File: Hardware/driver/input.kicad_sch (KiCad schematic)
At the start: 20 parts

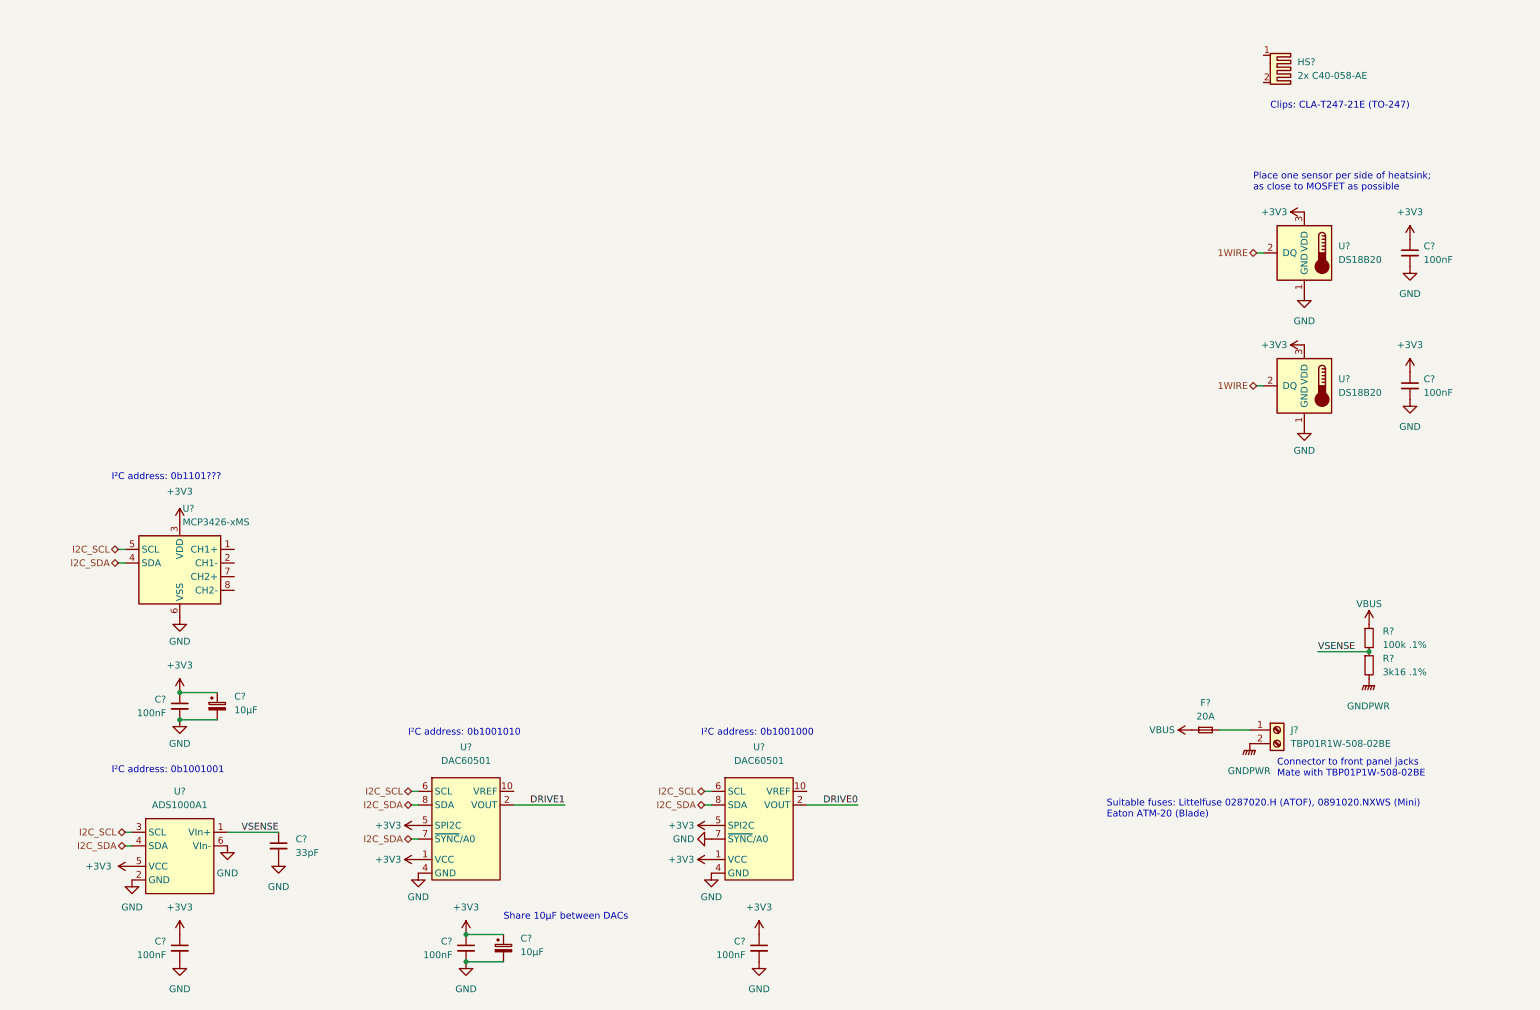
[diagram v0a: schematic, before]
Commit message: Basic board layout shape
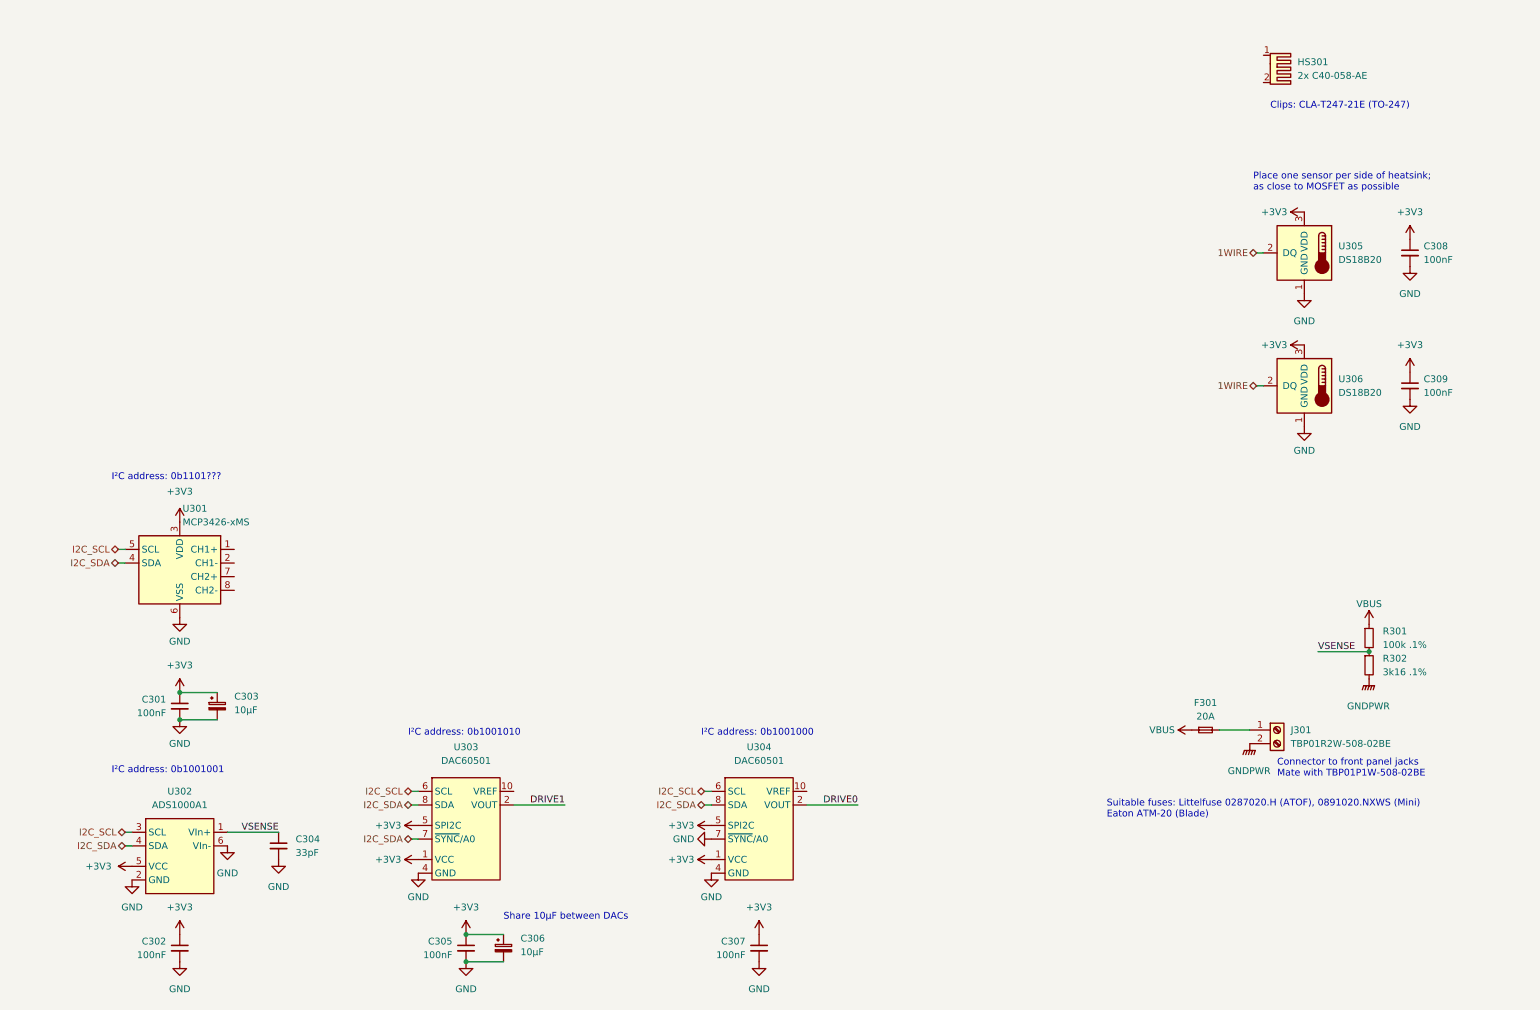
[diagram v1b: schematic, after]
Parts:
- J301: renamed from J?; value TBP01R1W-508-02BE -> TBP01R2W-508-02BE; footprint programmable-load:CUI_TBP01R1W-508-02BE -> programmable-load:CUI_TBP01R2W-508-02BE
- gave numbers to parts that had none: 19

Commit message: Added mains supply input
- The driver board contains a switching mains supply that will give us
  the 12V the system needs, as if by magic

- More work on layout, basically placed the output MOSFETs and stuff
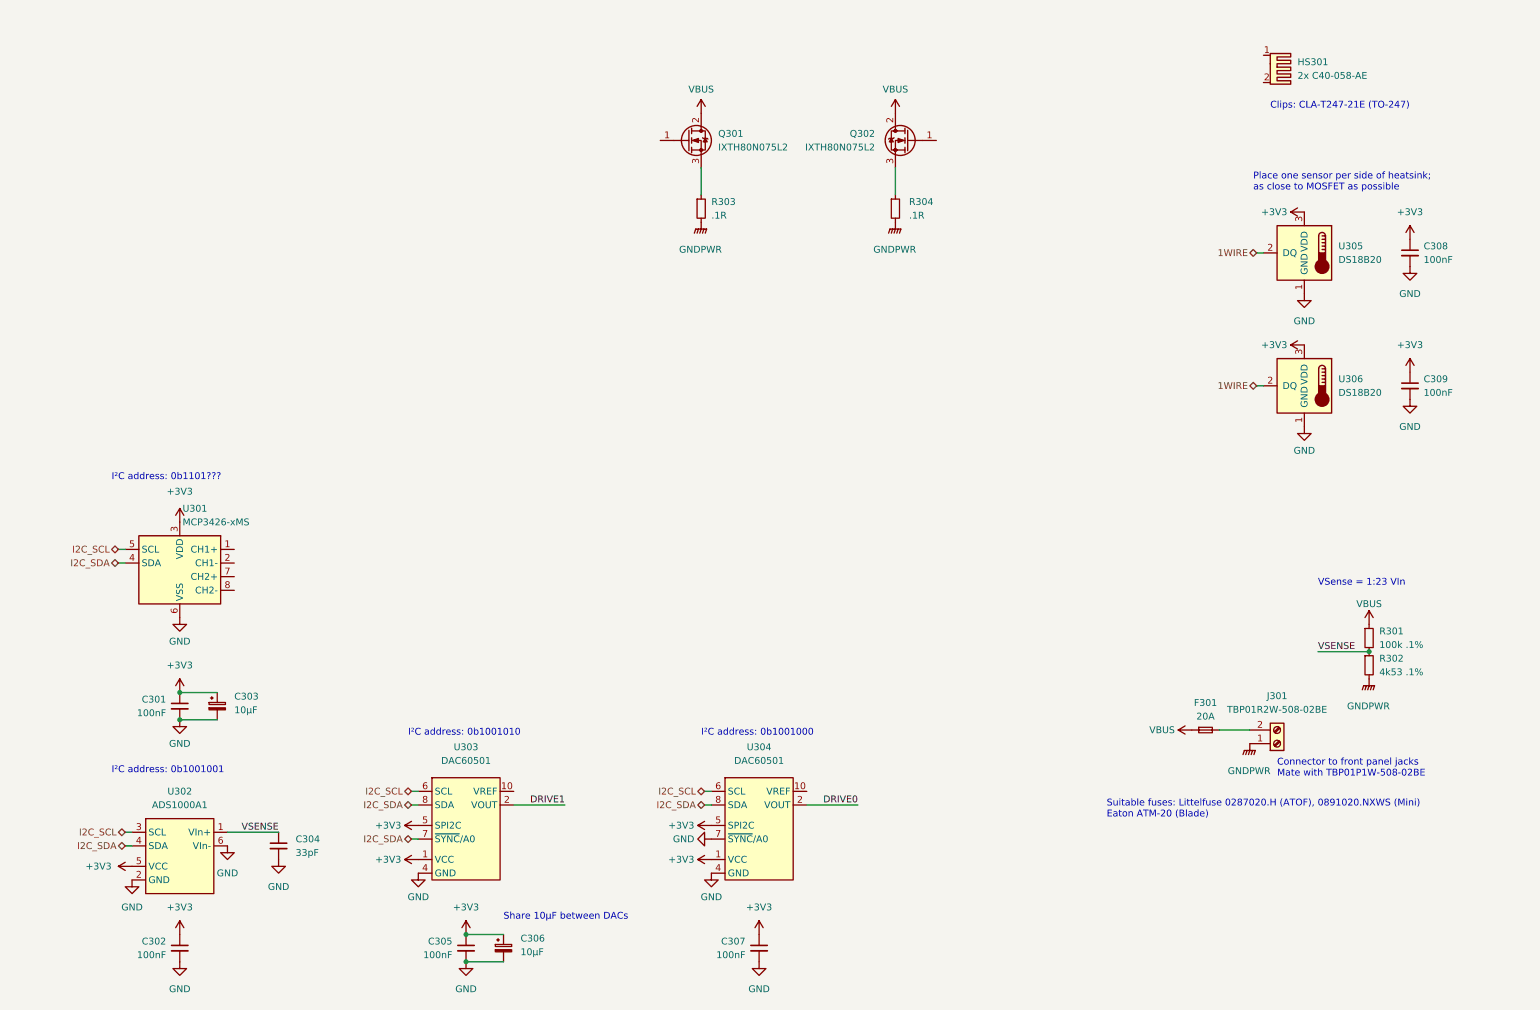
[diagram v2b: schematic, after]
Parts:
- added Q301, Q302: IXTH80N075L2, Package_TO_SOT_THT:TO-247-3_Vertical, symbol programmable-load:IXTH80N075L2
- added R303, R304: .1R, Package_TO_SOT_THT:TO-247-2_Vertical, symbol Device:R_Small
- C304: footprint (none) -> Capacitor_SMD:C_0805_2012Metric_Pad1.18x1.45mm_HandSolder
- R302: value 3k16 .1% -> 4k53 .1%; MPN RN732BTTD3161B25 -> ERA-8AEB4531V
- U301: footprint (none) -> Package_SO:MSOP-8_3x3mm_P0.65mm
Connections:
- net GNDPWR: now also J301.1 (Pin_1), R303.2, R304.2; no longer J301.2 (Pin_2)
- net VBUS: now also Q301.2 (D), Q302.2 (D)
- net at F301.2: now also J301.2 (Pin_2); no longer J301.1 (Pin_1)
- new net: Q302.3 (S), R304.1
- new net: Q301.3 (S), R303.1
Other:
- note added: "VSense = 1:23 VIn"
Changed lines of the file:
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@@
+    (stroke (width 0) (type default) (color 0 0 0 0))
+  )
+  (wire (pts (xy 141.605 42.545) (xy 141.605 47.625))
     (stroke (width 0) (type default) (color 0 0 0 0))
   )
@@
     (stroke (width 0) (type default) (color 0 0 0 0))
   )
+  (wire (pts (xy 177.8 42.545) (xy 177.8 47.625))
+    (stroke (width 0) (type default) (color 0 0 0 0))
+  )
   (text "I²C address: 0b1101???" (at 31.75 100.965 0)
     (effects (font (size 1.27 1.27)) (justify left bottom))
   )
   (text "I²C address: 0b1001010" (at 86.995 148.59 0)
+    (effects (font (size 1.27 1.27)) (justify left bottom))
+  )
+  (text "VSense = 1:23 VIn" (at 256.54 120.65 0)
     (effects (font (size 1.27 1.27)) (justify left bottom))
   )
@@
     (effects (font (size 1.27 1.27)) (justify right))
   )
+  (symbol (lib_id "Device:R_Small") (at 177.8 50.165 0) (unit 1)
+    (in_bom yes) (on_board yes) (fields_autoplaced)
+    (property "Reference" "R304" (id 0) (at 180.34 48.8949 0)
+      (effects (font (size 1.27 1.27)) (justify left))
+    )
+    (property "Value" ".1R" (id 1) (at 180.34 51.4349 0)
+      (effects (font (size 1.27 1.27)) (justify left))
+    )
+    (property "Footprint" "Package_TO_SOT_THT:TO-247-2_Vertical" (id 2) (at 177.8 50.165 0)
+      (effects (font (size 1.27 1.27)) hide)
+    )
+    (property "Datasheet" "~" (id 3) (at 177.8 50.165 0)
+      (effects (font (size 1.27 1.27)) hide)
+    )
+    (pin "1")
+    (pin "2")
+  )
   (symbol (lib_id "Device:C_Small") (at 62.865 168.91 0) (unit 1)
     (in_bom yes) (on_board yes) (fields_autoplaced)
@@
       (effects (font (size 1.27 1.27)) (justify left))
     )
-    (property "Footprint" "" (id 2) (at 62.865 168.91 0)
+    (property "Footprint" "Capacitor_SMD:C_0805_2012Metric_Pad1.18x1.45mm_HandSolder" (id 2) (at 62.865 168.91 0)
       (effects (font (size 1.27 1.27)) hide)
     )
@@
   (symbol (lib_id "Device:R_Small") (at 266.065 130.175 0) (unit 1)
     (in_bom yes) (on_board yes) (fields_autoplaced)
-    (property "Reference" "R301" (id 0) (at 268.605 128.9049 0)
-      (effects (font (size 1.27 1.27)) (justify left))
-    )
-    (property "Value" "100k .1%" (id 1) (at 268.605 131.4449 0)
+    (property "Reference" "R301" (id 0) (at 267.97 128.9049 0)
+      (effects (font (size 1.27 1.27)) (justify left))
+    )
+    (property "Value" "100k .1%" (id 1) (at 267.97 131.4449 0)
       (effects (font (size 1.27 1.27)) (justify left))
     )
@@
     (pin "1")
     (pin "2")
+  )
+  (symbol (lib_id "power:VBUS") (at 177.8 32.385 0) (unit 1)
+    (in_bom yes) (on_board yes)
+    (property "Reference" "#PWR0114" (id 0) (at 177.8 36.195 0)
+      (effects (font (size 1.27 1.27)) hide)
+    )
+    (property "Value" "VBUS" (id 1) (at 177.8 27.94 0))
+    (property "Footprint" "" (id 2) (at 177.8 32.385 0)
+      (effects (font (size 1.27 1.27)) hide)
+    )
+    (property "Datasheet" "" (id 3) (at 177.8 32.385 0)
+      (effects (font (size 1.27 1.27)) hide)
+    )
+    (pin "1")
+  )
+  (symbol (lib_id "programmable-load:IXTH80N075L2") (at 139.065 37.465 0) (unit 1)
+    (in_bom yes) (on_board yes) (fields_autoplaced)
+    (property "Reference" "Q301" (id 0) (at 144.78 36.1949 0)
+      (effects (font (size 1.27 1.27)) (justify left))
+    )
+    (property "Value" "IXTH80N075L2" (id 1) (at 144.78 38.7349 0)
+      (effects (font (size 1.27 1.27)) (justify left))
+    )
+    (property "Footprint" "Package_TO_SOT_THT:TO-247-3_Vertical" (id 2) (at 144.145 34.925 0)
+      (effects (font (size 1.27 1.27)) hide)
+    )
+    (property "Datasheet" "https://www.littelfuse.com/media?resourcetype=datasheets&itemid=88506b9c-8cbf-47b3-ba4a-fbdb5672fed3&filename=littelfuse-discrete-mosfets-n-channel-linear-ixt-80n075-datasheet" (id 3) (at 139.065 37.465 0)
+      (effects (font (size 1.27 1.27)) hide)
+    )
+    (pin "1")
+    (pin "2")
+    (pin "3")
   )
   (symbol (lib_id "programmable-load:DAC60501") (at 152.4 156.21 0) (unit 1)
@@
     (pin "1")
   )
+  (symbol (lib_id "Device:R_Small") (at 141.605 50.165 0) (unit 1)
+    (in_bom yes) (on_board yes) (fields_autoplaced)
+    (property "Reference" "R303" (id 0) (at 143.51 48.8949 0)
+      (effects (font (size 1.27 1.27)) (justify left))
+    )
+    (property "Value" ".1R" (id 1) (at 143.51 51.4349 0)
+      (effects (font (size 1.27 1.27)) (justify left))
+    )
+    (property "Footprint" "Package_TO_SOT_THT:TO-247-2_Vertical" (id 2) (at 141.605 50.165 0)
+      (effects (font (size 1.27 1.27)) hide)
+    )
+    (property "Datasheet" "~" (id 3) (at 141.605 50.165 0)
+      (effects (font (size 1.27 1.27)) hide)
+    )
+    (pin "1")
+    (pin "2")
+  )
+  (symbol (lib_id "power:GNDPWR") (at 177.8 52.705 0) (unit 1)
+    (in_bom yes) (on_board yes) (fields_autoplaced)
+    (property "Reference" "#PWR0115" (id 0) (at 177.8 57.785 0)
+      (effects (font (size 1.27 1.27)) hide)
+    )
+    (property "Value" "GNDPWR" (id 1) (at 177.673 57.785 0))
+    (property "Footprint" "" (id 2) (at 177.8 53.975 0)
+      (effects (font (size 1.27 1.27)) hide)
+    )
+    (property "Datasheet" "" (id 3) (at 177.8 53.975 0)
+      (effects (font (size 1.27 1.27)) hide)
+    )
+    (pin "1")
+  )
   (symbol (lib_id "Device:Fuse_Small") (at 235.585 147.32 0) (unit 1)
     (in_bom yes) (on_board yes) (fields_autoplaced)
@@
     (pin "1")
   )
-  (symbol (lib_id "Connector:Screw_Terminal_01x02") (at 248.92 147.32 0) (unit 1)
-    (in_bom yes) (on_board yes) (fields_autoplaced)
-    (property "Reference" "J301" (id 0) (at 251.46 147.3199 0)
-      (effects (font (size 1.27 1.27)) (justify left))
-    )
-    (property "Value" "TBP01R2W-508-02BE" (id 1) (at 251.46 149.8599 0)
-      (effects (font (size 1.27 1.27)) (justify left))
-    )
-    (property "Footprint" "programmable-load:CUI_TBP01R2W-508-02BE" (id 2) (at 248.92 147.32 0)
-      (effects (font (size 1.27 1.27)) hide)
-    )
-    (property "Datasheet" "~" (id 3) (at 248.92 147.32 0)
+  (symbol (lib_id "Connector:Screw_Terminal_01x02") (at 248.92 149.86 0) (mirror x) (unit 1)
+    (in_bom yes) (on_board yes) (fields_autoplaced)
+    (property "Reference" "J301" (id 0) (at 248.92 140.97 0))
+    (property "Value" "TBP01R2W-508-02BE" (id 1) (at 248.92 143.51 0))
+    (property "Footprint" "programmable-load:CUI_TBP01R2W-508-02BE" (id 2) (at 248.92 149.86 0)
+      (effects (font (size 1.27 1.27)) hide)
+    )
+    (property "Datasheet" "~" (id 3) (at 248.92 149.86 0)
       (effects (font (size 1.27 1.27)) hide)
     )
@@
     )
     (pin "1")
+  )
+  (symbol (lib_id "programmable-load:IXTH80N075L2") (at 180.34 37.465 0) (mirror y) (unit 1)
+    (in_bom yes) (on_board yes) (fields_autoplaced)
+    (property "Reference" "Q302" (id 0) (at 173.99 36.1949 0)
+      (effects (font (size 1.27 1.27)) (justify left))
+    )
+    (property "Value" "IXTH80N075L2" (id 1) (at 173.99 38.7349 0)
+      (effects (font (size 1.27 1.27)) (justify left))
+    )
+    (property "Footprint" "Package_TO_SOT_THT:TO-247-3_Vertical" (id 2) (at 175.26 34.925 0)
+      (effects (font (size 1.27 1.27)) hide)
+    )
+    (property "Datasheet" "https://www.littelfuse.com/media?resourcetype=datasheets&itemid=88506b9c-8cbf-47b3-ba4a-fbdb5672fed3&filename=littelfuse-discrete-mosfets-n-channel-linear-ixt-80n075-datasheet" (id 3) (at 180.34 37.465 0)
+      (effects (font (size 1.27 1.27)) hide)
+    )
+    (pin "1")
+    (pin "2")
+    (pin "3")
   )
   (symbol (lib_id "power:+3V3") (at 44.45 185.42 0) (unit 1)
@@
     )
     (property "Datasheet" "" (id 3) (at 143.51 167.64 0)
+      (effects (font (size 1.27 1.27)) hide)
+    )
+    (pin "1")
+  )
+  (symbol (lib_id "power:GNDPWR") (at 141.605 52.705 0) (unit 1)
+    (in_bom yes) (on_board yes) (fields_autoplaced)
+    (property "Reference" "#PWR0112" (id 0) (at 141.605 57.785 0)
+      (effects (font (size 1.27 1.27)) hide)
+    )
+    (property "Value" "GNDPWR" (id 1) (at 141.478 57.785 0))
+    (property "Footprint" "" (id 2) (at 141.605 53.975 0)
+      (effects (font (size 1.27 1.27)) hide)
+    )
+    (property "Datasheet" "" (id 3) (at 141.605 53.975 0)
       (effects (font (size 1.27 1.27)) hide)
     )
@@
       (effects (font (size 1.27 1.27)) (justify right))
     )
-    (property "Footprint" "" (id 2) (at 44.45 118.745 0)
+    (property "Footprint" "Package_SO:MSOP-8_3x3mm_P0.65mm" (id 2) (at 44.45 118.745 0)
       (effects (font (size 1.27 1.27)) hide)
     )
@@
   (symbol (lib_id "Device:R_Small") (at 266.065 135.255 0) (unit 1)
     (in_bom yes) (on_board yes) (fields_autoplaced)
-    (property "Reference" "R302" (id 0) (at 268.605 133.9849 0)
-      (effects (font (size 1.27 1.27)) (justify left))
-    )
-    (property "Value" "3k16 .1%" (id 1) (at 268.605 136.5249 0)
+    (property "Reference" "R302" (id 0) (at 267.97 133.9849 0)
+      (effects (font (size 1.27 1.27)) (justify left))
+    )
+    (property "Value" "4k53 .1%" (id 1) (at 267.97 136.5249 0)
       (effects (font (size 1.27 1.27)) (justify left))
     )
@@
       (effects (font (size 1.27 1.27)) hide)
     )
-    (property "MPN" "RN732BTTD3161B25" (id 4) (at 266.065 135.255 0)
+    (property "MPN" "ERA-8AEB4531V" (id 4) (at 266.065 135.255 0)
       (effects (font (size 1.27 1.27)) hide)
     )
@@
       (effects (font (size 1.27 1.27)) hide)
     )
+    (pin "1")
+  )
+  (symbol (lib_id "power:VBUS") (at 141.605 32.385 0) (unit 1)
+    (in_bom yes) (on_board yes)
+    (property "Reference" "#PWR0113" (id 0) (at 141.605 36.195 0)
+      (effects (font (size 1.27 1.27)) hide)
+    )
+    (property "Value" "VBUS" (id 1) (at 141.605 27.94 0))
+    (property "Footprint" "" (id 2) (at 141.605 32.385 0)
+      (effects (font (size 1.27 1.27)) hide)
+    )
+    (property "Datasheet" "" (id 3) (at 141.605 32.385 0)
+      (effects (font (size 1.27 1.27)) hide)
+    )
